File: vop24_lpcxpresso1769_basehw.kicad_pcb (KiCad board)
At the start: 2 copper layers, 113 parts, among them J1 Micro_SD_Card, J101 Conn_01x03_Male, J201 Screw_Terminal_01x02, J301 USB_B_Micro, J302 Conn_01x06_Male, J303 Conn_01x05_Male, J304 Screw_Terminal_01x02, J401 Conn_01x02, J402 Conn_01x02, J403 Conn_01x02, J404 Conn_01x04, J405 Conn_01x04, J406 Conn_01x04, U1 LPCXpresso1769, U101 MCP1700T-3302E_TT, U102 MCP1700T-3302E_TT, U103 TPS63001, U201 LM358, U301 TPD4S014, U302 LTC4411, U303 LT1512, U401 ADS1292, U402 LM334, U403 LM334, U404 LM334

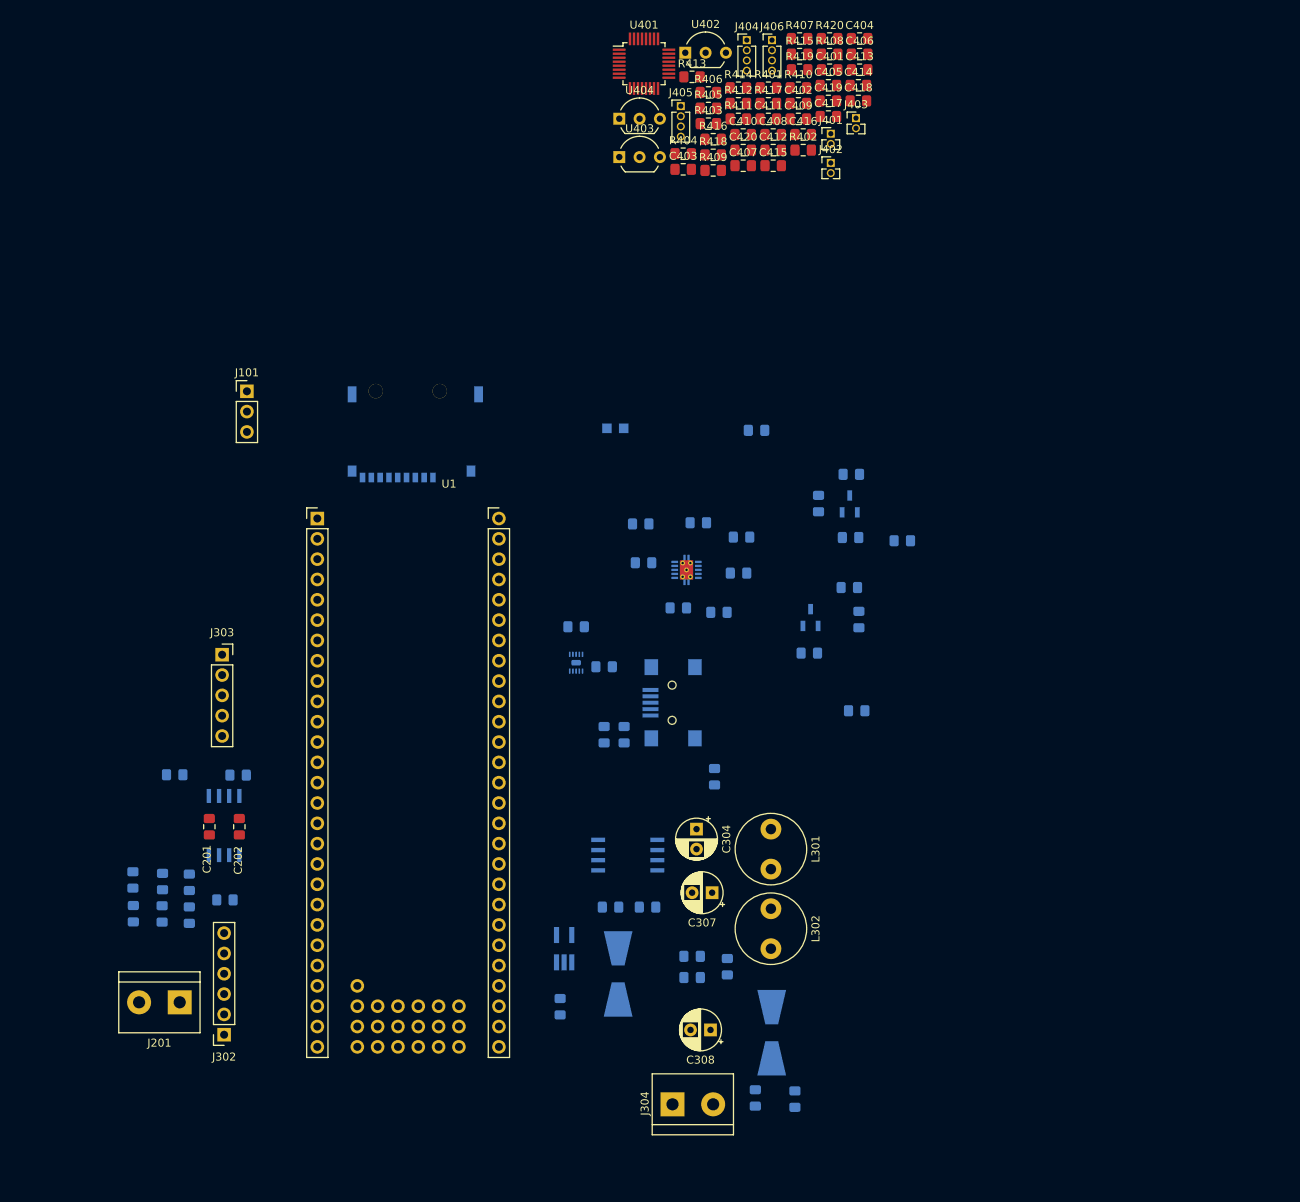
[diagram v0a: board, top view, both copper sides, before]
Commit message: PCB: componentes agrupados por zona
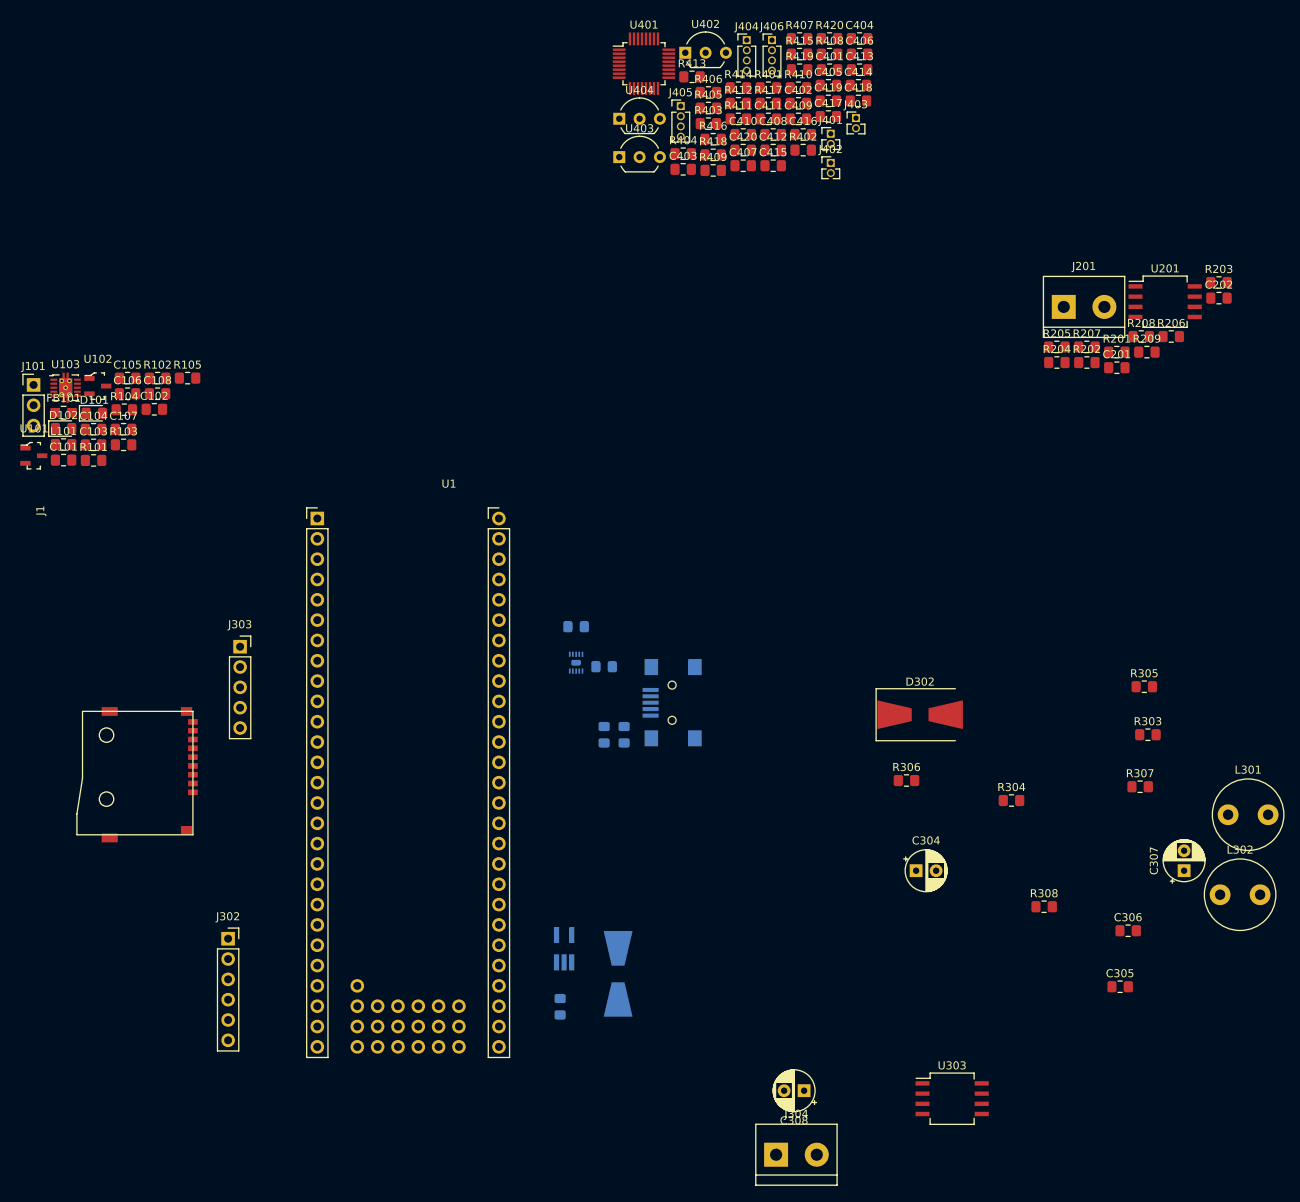
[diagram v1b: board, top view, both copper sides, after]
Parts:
- C101, C102, C103, C104, C105, C106, C107, C108, C305, C306, D101, D102, D302, FB101, J1, L101, R101, R102, R103, R104, R105, R201, R202, R203, R204, R205, R206, R207, R208, R209, R303, R304, R305, R306, R307, R308, U101, U102, U103, U201, U303: moved to F.Cu
- moved R203 144.3 mm to (192.4, 76.0)
- moved R206 143.3 mm to (186.4, 82.7), turned to 0 degrees
- moved J201 140.6 mm to (173.0, 79.0), turned to 0 degrees
- moved R201 139.6 mm to (179.6, 84.7), turned to 0 degrees
- moved R208 139.3 mm to (182.6, 82.7), turned to 0 degrees
- moved C202 139.1 mm to (192.4, 77.9), turned to 0 degrees
- moved R209 136.8 mm to (183.3, 84.7), turned to 0 degrees
- moved U201 134.6 mm to (185.6, 78.4), turned to 0 degrees
- moved R204 134.4 mm to (172.1, 86.0), turned to 0 degrees
- moved R205 132.4 mm to (172.1, 84.0), turned to 0 degrees
- moved R207 128.0 mm to (175.8, 84.0), turned to 0 degrees
- moved C201 127.1 mm to (179.6, 86.6), turned to 0 degrees
- moved R202 118.0 mm to (175.8, 86.0)
- moved D102 105.8 mm to (47.9, 94.2)
- moved U101 102.2 mm to (44.2, 97.6), turned to 0 degrees
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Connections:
- C412 pad 2: /ADS1292_esquematico/SENS1N -> /ADS1292_esquematico/SENS1P
- C413 pad 2: /ADS1292_esquematico/SENS2N -> /ADS1292_esquematico/SENS2P
- C414 pad 2: /ADS1292_esquematico/SENS3N -> /ADS1292_esquematico/SENS3P
- C416 pad 1: /ADS1292_esquematico/SENS1N -> /ADS1292_esquematico/SENS1P
- C418 pad 1: /ADS1292_esquematico/SENS2N -> /ADS1292_esquematico/SENS2P
- C420 pad 1: /ADS1292_esquematico/SENS3N -> /ADS1292_esquematico/SENS3P
- R416 pad 1: /ADS1292_esquematico/SENS1N -> /ADS1292_esquematico/SENS1P
- R418 pad 1: /ADS1292_esquematico/SENS2N -> /ADS1292_esquematico/SENS2P
- R420 pad 1: /ADS1292_esquematico/SENS3N -> /ADS1292_esquematico/SENS3P
